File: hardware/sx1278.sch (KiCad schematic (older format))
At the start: 4 parts

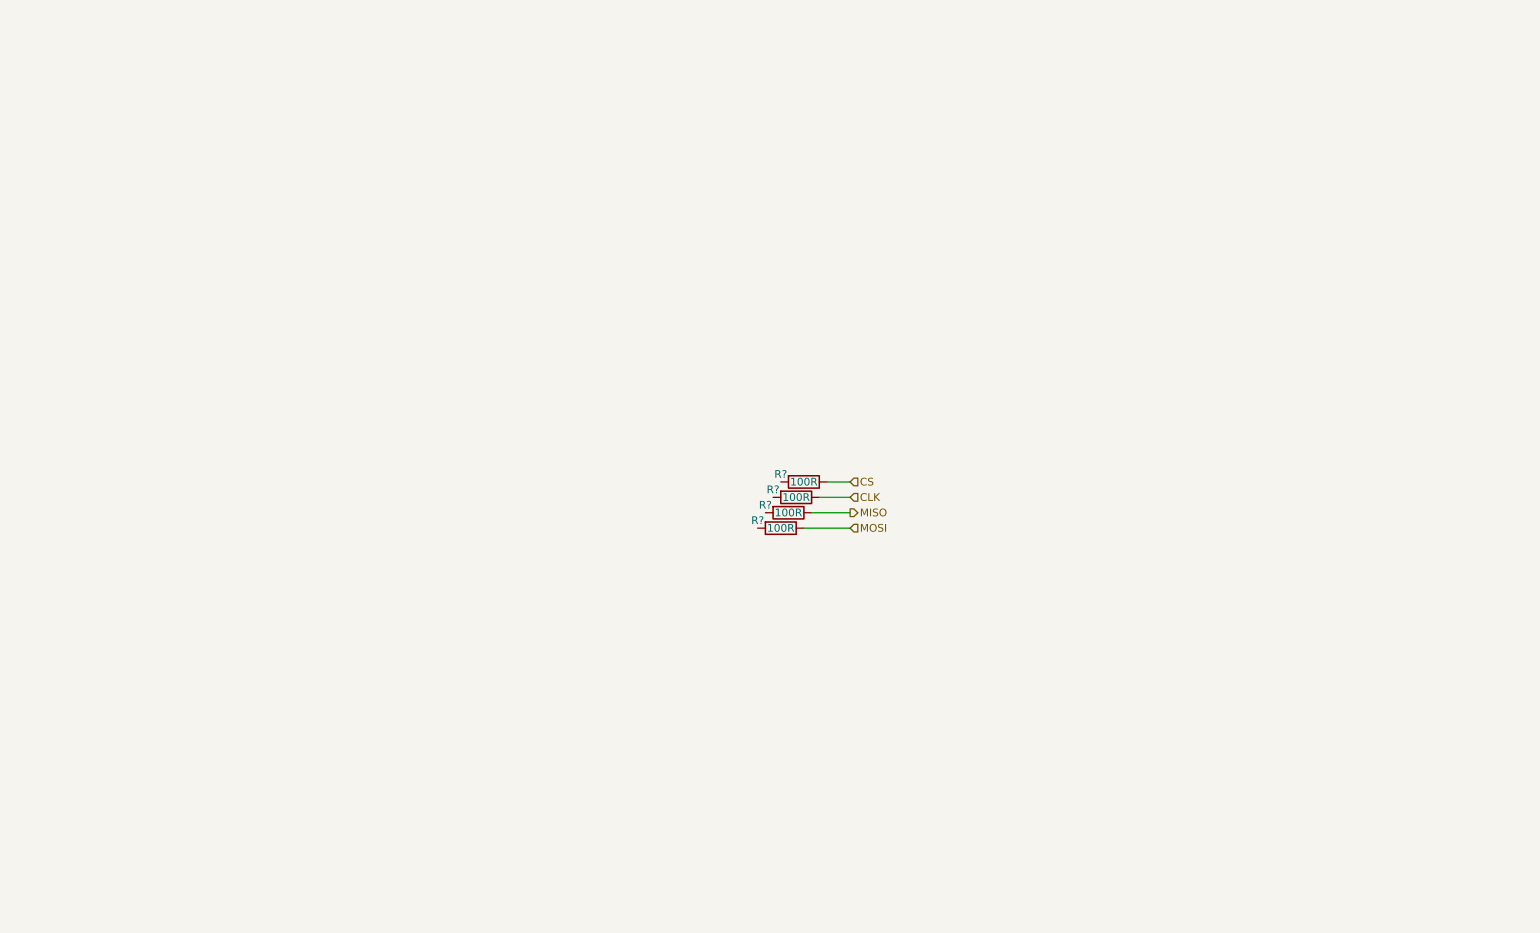
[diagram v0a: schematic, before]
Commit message: Finished sx1278 schematic
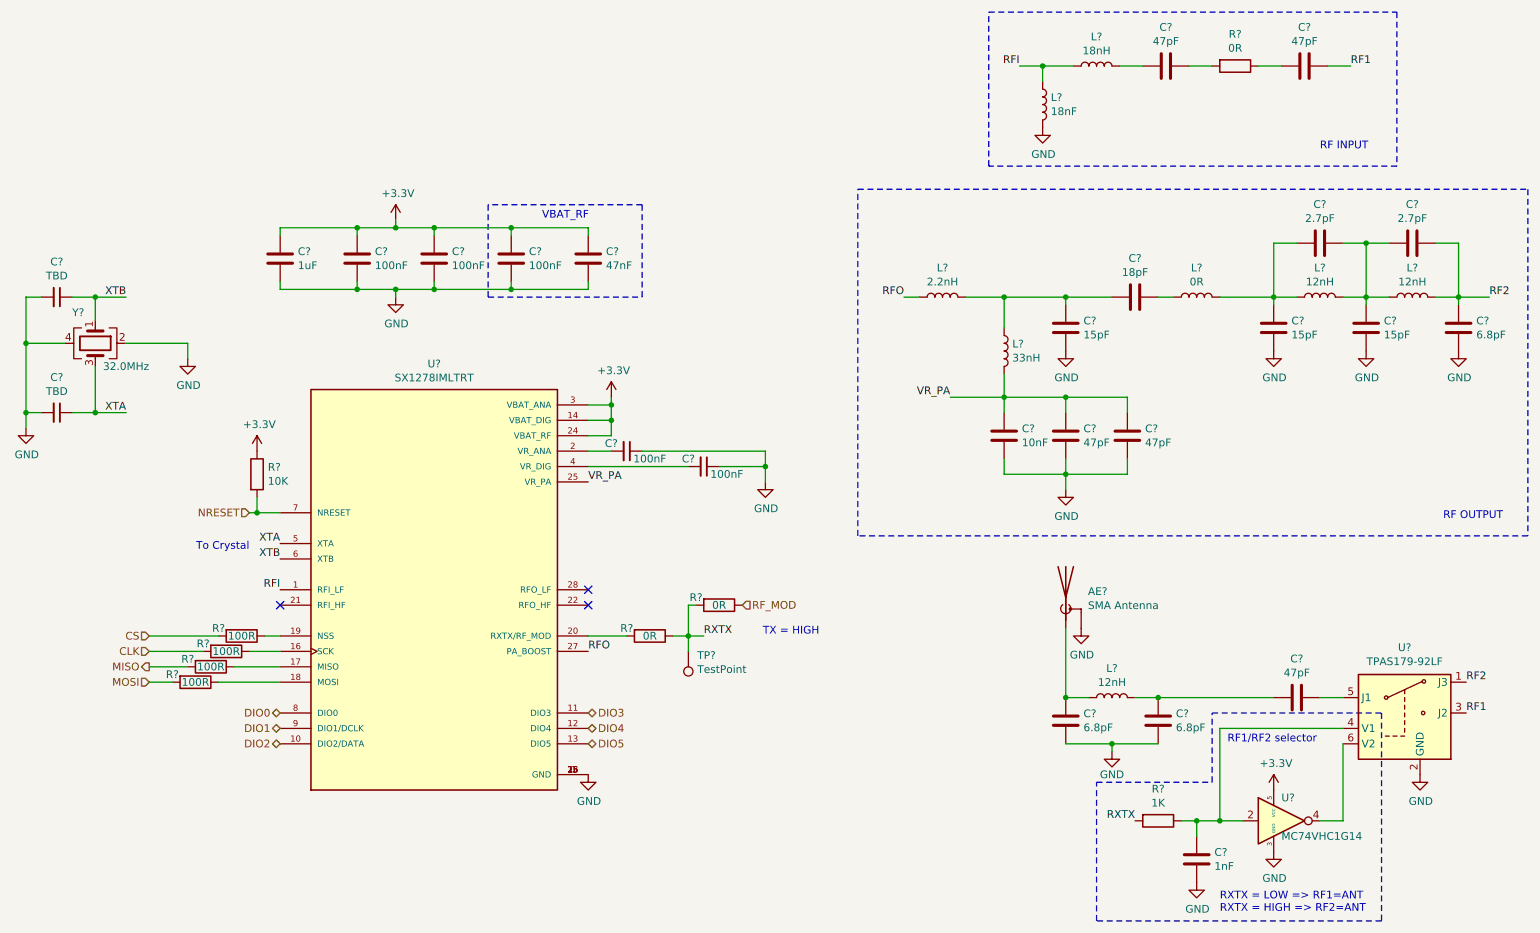
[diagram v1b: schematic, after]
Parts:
- added AE?: SMA Antenna, symbol Device:Antenna_Shield
- added C? (x2): TBD, symbol Device:C_Small
- added C? (x2): 100nF, symbol Device:C_Small
- added C?: 1uF, symbol Device:C
- added C? (x3): 100nF, symbol Device:C
- added C?: 1nF, symbol Device:C
- added C? (x5): 47pF, symbol Device:C
- added C? (x3): 6.8pF, symbol Device:C
- added C?: 10nF, symbol Device:C
- added C?: 47nF, symbol Device:C
- added C? (x3): 15pF, symbol Device:C
- added C?: 18pF, symbol Device:C
- added C? (x2): 2.7pF, symbol Device:C
- added L? (x3): 12nH, symbol Device:L
- added L?: 18nF, symbol Device:L
- added L?: 18nH, symbol Device:L
- added L?: 33nH, symbol Device:L
- added L?: 2.2nH, symbol Device:L
- added L?: 0R, symbol Device:L
- added R?: 10K, symbol Device:R
- added R?: 1K, symbol Device:R
- added R? (x3): 0R, symbol Device:R
- added TP?: TestPoint, symbol Connector:TestPoint
- added U?: SX1278IMLTRT, QFN65P600X600X100-29N, symbol sx1278:SX1278IMLTRT
- added U?: TPAS179-92LF, Package_TO_SOT_SMD:SOT-363_SC-70-6, symbol RF_Switch:AS179-92LF
- added U?: MC74VHC1G14, Package_TO_SOT_SMD:SOT-353_SC-70-5, symbol 74xGxx:NC7SVU04P5X
- added Y?: 32.0MHz, symbol Device:Crystal_GND24
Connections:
- net CLK: now also R?.2; no longer R?.1
- net CS: now also R?.2; no longer R?.1
- net MISO: now also R?.2; no longer R?.1
- net MOSI: now also R?.2; no longer R?.1
- new net: R?.1, U?.16 (SCK)
- new net: R?.1, U?.17 (MISO)
- new net: R?.1, U?.18 (MOSI)
- new net: R?.1, U?.19 (NSS)
- new net: C?.2, U?.2 (VR_ANA)
- new net: R?.2, U?.20 (RXTX/RF_MOD)
- new net: C?.2, U?.4 (VR_DIG)
- new net: AE?.1 (A), C?.1, L?.1
- new net: C?.1, R?.1, U?.2, U?.4 (V1)
- new net: C?.1, U?.5 (J1)
- new net: U?.4, U?.6 (V2)
- new net: C?.1, C?.2, L?.2
- new net: C?.2, L?.2
- new net: C?.1, R?.2
- new net: C?.2, R?.1
- new net: C?.1, C?.2, L?.1, L?.2 (x2)
- new net: C?.1, L?.1
- new net: C?.1, C?.1, C?.2, L?.1, L?.2
- new net +3V3: C?.1, C?.1, C?.1, C?.1, C?.1, R?.1, U?.14 (VBAT_DIG), U?.24 (VBAT_RF), U?.3 (VBAT_ANA), U?.5 (VCC)
- new net DIO0: U?.8 (DIO0)
- new net DIO1: U?.9 (DIO1/DCLK)
- new net DIO2: U?.10 (DIO2/DATA)
- new net DIO3: U?.11 (DIO3)
- new net DIO4: U?.12 (DIO4)
- new net DIO5: U?.13 (DIO5)
- new net GND: AE?.2 (Shield), C?.1, C?.1, C?.2, C?.2, C?.2, C?.2, C?.2, C?.2, C?.2, C?.2, C?.2, C?.2, C?.2, C?.2, C?.2, C?.2, C?.2, C?.2, C?.2, L?.2, U?.0 (GND), U?.15 (GND), U?.2 (GND), U?.23 (GND), U?.26 (GND), U?.3 (GND), Y?.2, Y?.4
- new net NRESET: R?.2, U?.7 (NRESET)
- new net RF1: C?.1, U?.3 (J2)
- new net RF2: C?.1, C?.1, L?.2, U?.1 (J3)
- new net RFI: L?.1, L?.1, U?.1 (RFI_LF)
- new net RFO: L?.1, U?.27 (PA_BOOST)
- new net RF_MOD: R?.1
- new net RXTX: R?.1, R?.2, R?.2, TP?.1
- new net VR_PA: C?.1, C?.1, C?.1, L?.2, U?.25 (VR_PA)
- new net XTA: C?.1, U?.5 (XTA), Y?.3
- new net XTB: C?.1, U?.6 (XTB), Y?.1
- no-connect marks 0 -> 3
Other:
- note added: "RF INPUT"
- note added: "RF OUTPUT"
- note added: "RF1/RF2 selector"
- note added: "RXTX = LOW => RF1=ANT\nRXTX = HIGH => RF2=ANT"
- note added: "TX = HIGH"
- note added: "To Crystal"
- note added: "VBAT_RF"
- moved on the sheet: R?

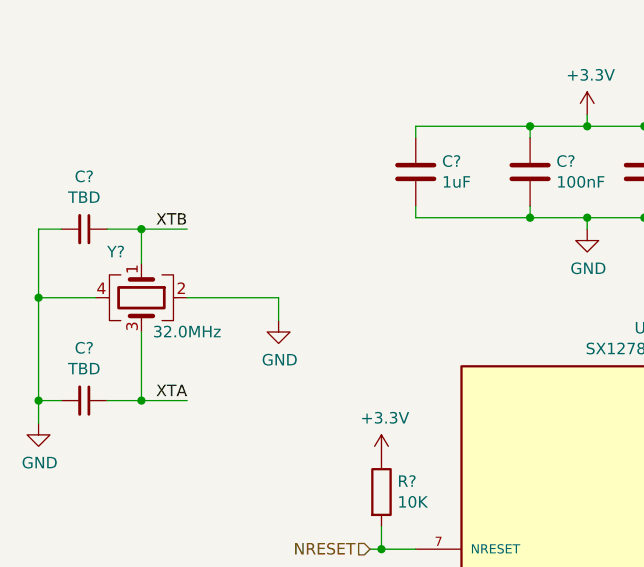
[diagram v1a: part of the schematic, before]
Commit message: Select crystals, add HSE for stm32 and fixed some bits
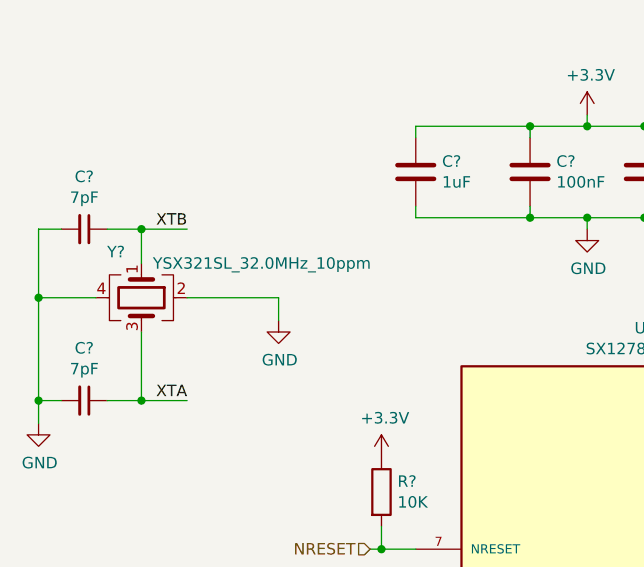
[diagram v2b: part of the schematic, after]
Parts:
- C? (x2): value TBD -> 7pF
- Y?: value 32.0MHz -> YSX321SL_32.0MHz_10ppm; footprint (none) -> Crystal:Crystal_SMD_3225-4Pin_3.2x2.5mm
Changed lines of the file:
@@
 encoding utf-8
 Sheet 4 5
-Title ""
+Title "Meteostation"
 Date ""
 Rev ""
-Comp ""
+Comp "Technospark"
 Comment1 ""
-Comment2 ""
+Comment2 "Aleksul"
 Comment3 ""
 Comment4 ""
@@
 	2150 4900 2550 4900
 $Comp
-L power:GND #PWR?
+L power:GND #PWR0172
 U 1 1 607BCAFD
 P 4550 5500
-F 0 "#PWR?" H 4550 5250 50  0001 C CNN
+F 0 "#PWR0172" H 4550 5250 50  0001 C CNN
 F 1 "GND" H 4555 5327 50  0000 C CNN
 F 2 "" H 4550 5500 50  0001 C CNN
@@
 $EndComp
 $Comp
-L power:+3.3V #PWR?
+L power:+3.3V #PWR0173
 U 1 1 607D9E51
 P 2400 3400
-F 0 "#PWR?" H 2400 3250 50  0001 C CNN
+F 0 "#PWR0173" H 2400 3250 50  0001 C CNN
 F 1 "+3.3V" H 2415 3573 50  0000 C CNN
 F 2 "" H 2400 3400 50  0001 C CNN
@@
 P 1100 3150
 F 0 "C?" V 871 3150 50  0000 C CNN
-F 1 "TBD" V 962 3150 50  0000 C CNN
+F 1 "7pF" V 962 3150 50  0000 C CNN
 F 2 "" H 1100 3150 50  0001 C CNN
 F 3 "~" H 1100 3150 50  0001 C CNN
@@
 P 1100 2400
 F 0 "C?" V 871 2400 50  0000 C CNN
-F 1 "TBD" V 962 2400 50  0000 C CNN
+F 1 "7pF" V 962 2400 50  0000 C CNN
 F 2 "" H 1100 2400 50  0001 C CNN
 F 3 "~" H 1100 2400 50  0001 C CNN
@@
 P 1350 2700
 F 0 "Y?" V 1150 2550 50  0000 L CNN
-F 1 "32.0MHz" V 1500 2750 50  0000 L CNN
-F 2 "" H 1350 2700 50  0001 C CNN
+F 1 "YSX321SL_32.0MHz_10ppm" V 1200 2750 50  0000 L CNN
+F 2 "Crystal:Crystal_SMD_3225-4Pin_3.2x2.5mm" H 1350 2700 50  0001 C CNN
 F 3 "~" H 1350 2700 50  0001 C CNN
 	1    1350 2700
@@
 Connection ~ 1350 2400
 $Comp
-L power:GND #PWR?
+L power:GND #PWR0174
 U 1 1 607F6B66
 P 1950 2800
-F 0 "#PWR?" H 1950 2550 50  0001 C CNN
+F 0 "#PWR0174" H 1950 2550 50  0001 C CNN
 F 1 "GND" H 1955 2627 50  0000 C CNN
 F 2 "" H 1950 2800 50  0001 C CNN
@@
 	1950 2700 1550 2700
 $Comp
-L power:GND #PWR?
+L power:GND #PWR0175
 U 1 1 607FA960
 P 900 3250
-F 0 "#PWR?" H 900 3000 50  0001 C CNN
+F 0 "#PWR0175" H 900 3000 50  0001 C CNN
 F 1 "GND" H 905 3077 50  0000 C CNN
 F 2 "" H 900 3250 50  0001 C CNN
@@
 $EndComp
 $Comp
-L power:GND #PWR?
+L power:GND #PWR0176
 U 1 1 608065FD
 P 5700 3600
-F 0 "#PWR?" H 5700 3350 50  0001 C CNN
+F 0 "#PWR0176" H 5700 3350 50  0001 C CNN
 F 1 "GND" H 5705 3427 50  0000 C CNN
 F 2 "" H 5700 3600 50  0001 C CNN
@@
 $EndComp
 $Comp
-L power:+3.3V #PWR?
+L power:+3.3V #PWR0177
 U 1 1 6080AC31
 P 3300 1900
-F 0 "#PWR?" H 3300 1750 50  0001 C CNN
+F 0 "#PWR0177" H 3300 1750 50  0001 C CNN
 F 1 "+3.3V" H 3315 2073 50  0000 C CNN
 F 2 "" H 3300 1900 50  0001 C CNN
@@
 $EndComp
 $Comp
-L power:GND #PWR?
+L power:GND #PWR0178
 U 1 1 6080CCB3
 P 3300 2400
-F 0 "#PWR?" H 3300 2150 50  0001 C CNN
+F 0 "#PWR0178" H 3300 2150 50  0001 C CNN
 F 1 "GND" H 3305 2227 50  0000 C CNN
 F 2 "" H 3300 2400 50  0001 C CNN
@@
 Connection ~ 3050 1950
 $Comp
-L power:+3.3V #PWR?
+L power:+3.3V #PWR0179
 U 1 1 608179F3
 P 4700 3050
-F 0 "#PWR?" H 4700 2900 50  0001 C CNN
+F 0 "#PWR0179" H 4700 2900 50  0001 C CNN
 F 1 "+3.3V" H 4715 3223 50  0000 C CNN
 F 2 "" H 4700 3050 50  0001 C CNN
@@
 $EndComp
 $Comp
-L power:GND #PWR?
+L power:GND #PWR0180
 U 1 1 6083FC11
 P 7750 4550
-F 0 "#PWR?" H 7750 4300 50  0001 C CNN
+F 0 "#PWR0180" H 7750 4300 50  0001 C CNN
 F 1 "GND" H 7755 4377 50  0000 C CNN
 F 2 "" H 7750 4550 50  0001 C CNN
@@
 $EndComp
 $Comp
-L power:GND #PWR?
+L power:GND #PWR0181
 U 1 1 60845D96
 P 9950 5500
-F 0 "#PWR?" H 9950 5250 50  0001 C CNN
+F 0 "#PWR0181" H 9950 5250 50  0001 C CNN
 F 1 "GND" H 9955 5327 50  0000 C CNN
 F 2 "" H 9950 5500 50  0001 C CNN
@@
 $EndComp
 $Comp
-L power:GND #PWR?
+L power:GND #PWR0182
 U 1 1 6084BC05
 P 9000 6000
-F 0 "#PWR?" H 9000 5750 50  0001 C CNN
+F 0 "#PWR0182" H 9000 5750 50  0001 C CNN
 F 1 "GND" H 9005 5827 50  0000 C CNN
 F 2 "" H 9000 6000 50  0001 C CNN
@@
 $EndComp
 $Comp
-L power:+3.3V #PWR?
+L power:+3.3V #PWR0183
 U 1 1 6084BF68
 P 9000 5600
-F 0 "#PWR?" H 9000 5450 50  0001 C CNN
+F 0 "#PWR0183" H 9000 5450 50  0001 C CNN
 F 1 "+3.3V" H 9015 5773 50  0000 C CNN
 F 2 "" H 9000 5600 50  0001 C CNN
@@
 $EndComp
 $Comp
-L power:GND #PWR?
+L power:GND #PWR0184
 U 1 1 60862585
 P 8500 6200
-F 0 "#PWR?" H 8500 5950 50  0001 C CNN
+F 0 "#PWR0184" H 8500 5950 50  0001 C CNN
 F 1 "GND" H 8505 6027 50  0000 C CNN
 F 2 "" H 8500 6200 50  0001 C CNN
@@
 	8250 5000 9000 5000
 $Comp
-L power:GND #PWR?
+L power:GND #PWR0185
 U 1 1 608A4F1C
 P 7950 5350
-F 0 "#PWR?" H 7950 5100 50  0001 C CNN
+F 0 "#PWR0185" H 7950 5100 50  0001 C CNN
 F 1 "GND" H 7950 5200 50  0000 C CNN
 F 2 "" H 7950 5350 50  0001 C CNN
@@
 RF1
 $Comp
-L power:GND #PWR?
+L power:GND #PWR0186
 U 1 1 608B75C0
 P 7500 1300
-F 0 "#PWR?" H 7500 1050 50  0001 C CNN
+F 0 "#PWR0186" H 7500 1050 50  0001 C CNN
 F 1 "GND" H 7505 1127 50  0000 C CNN
 F 2 "" H 7500 1300 50  0001 C CNN
@@
 Connection ~ 7650 3050
 $Comp
-L power:GND #PWR?
+L power:GND #PWR0187
 U 1 1 608E8BAF
 P 7650 3650
-F 0 "#PWR?" H 7650 3400 50  0001 C CNN
+F 0 "#PWR0187" H 7650 3400 50  0001 C CNN
 F 1 "GND" H 7655 3477 50  0000 C CNN
 F 2 "" H 7650 3650 50  0001 C CNN
@@
 $EndComp
 $Comp
-L power:GND #PWR?
+L power:GND #PWR0188
 U 1 1 60909ED7
 P 7650 2750
-F 0 "#PWR?" H 7650 2500 50  0001 C CNN
+F 0 "#PWR0188" H 7650 2500 50  0001 C CNN
 F 1 "GND" H 7655 2577 50  0000 C CNN
 F 2 "" H 7650 2750 50  0001 C CNN
@@
 Connection ~ 10200 2400
 $Comp
-L power:GND #PWR?
+L power:GND #PWR0189
 U 1 1 609445A2
 P 9000 2750
-F 0 "#PWR?" H 9000 2500 50  0001 C CNN
+F 0 "#PWR0189" H 9000 2500 50  0001 C CNN
 F 1 "GND" H 9005 2577 50  0000 C CNN
 F 2 "" H 9000 2750 50  0001 C CNN
@@
 $EndComp
 $Comp
-L power:GND #PWR?
+L power:GND #PWR0190
 U 1 1 60945D29
 P 9600 2750
-F 0 "#PWR?" H 9600 2500 50  0001 C CNN
+F 0 "#PWR0190" H 9600 2500 50  0001 C CNN
 F 1 "GND" H 9605 2577 50  0000 C CNN
 F 2 "" H 9600 2750 50  0001 C CNN
@@
 $EndComp
 $Comp
-L power:GND #PWR?
+L power:GND #PWR0191
 U 1 1 6094646B
 P 10200 2750
-F 0 "#PWR?" H 10200 2500 50  0001 C CNN
+F 0 "#PWR0191" H 10200 2500 50  0001 C CNN
 F 1 "GND" H 10205 2577 50  0000 C CNN
 F 2 "" H 10200 2750 50  0001 C CNN

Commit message: Annotation complete
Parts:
- gave numbers to parts that had none: 48

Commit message: Finish adding footprints
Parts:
- AE2: footprint (none) -> Connector_Coaxial:SMA_Molex_73251-2200_Horizontal
- C35, C36, C37, C38, C40, C41, C42, C43, C44, C45, C46, C47, C48, C49, C50, C51, C52, C53, C54, C55, C56, C57, C58, C59: footprint (none) -> Capacitor_SMD:C_0805_2012Metric
- C39: footprint (none) -> Capacitor_SMD:C_1206_3216Metric
- L10, L11, L4, L6, L8, L9: footprint (none) -> Inductor_SMD:L_0603_1608Metric
- L5: value 18nF -> 18nH; footprint (none) -> Inductor_SMD:L_0603_1608Metric
- L7, R45, R47, R49: footprint (none) -> Resistor_SMD:R_2512_6332Metric
- R46, R48, R50, R51, R52, R53: footprint (none) -> Resistor_SMD:R_0805_2012Metric
- TP1: footprint (none) -> TestPoint:TestPoint_Pad_D2.5mm
- U8: footprint QFN65P600X600X100-29N -> libs:QFN65P600X600X100-29N

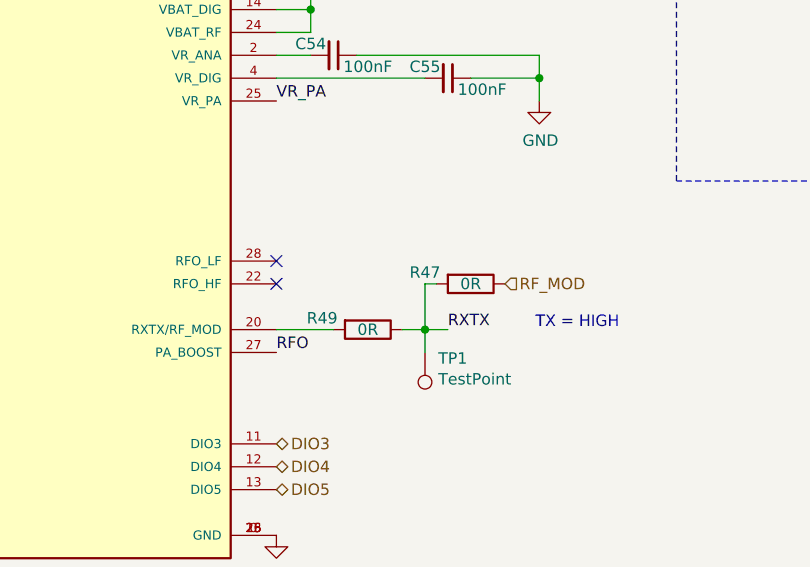
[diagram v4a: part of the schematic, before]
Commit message: Change 0Rto solder jumpers Add 3d model for bq25895 Fix button pcb model Start power part of pcb
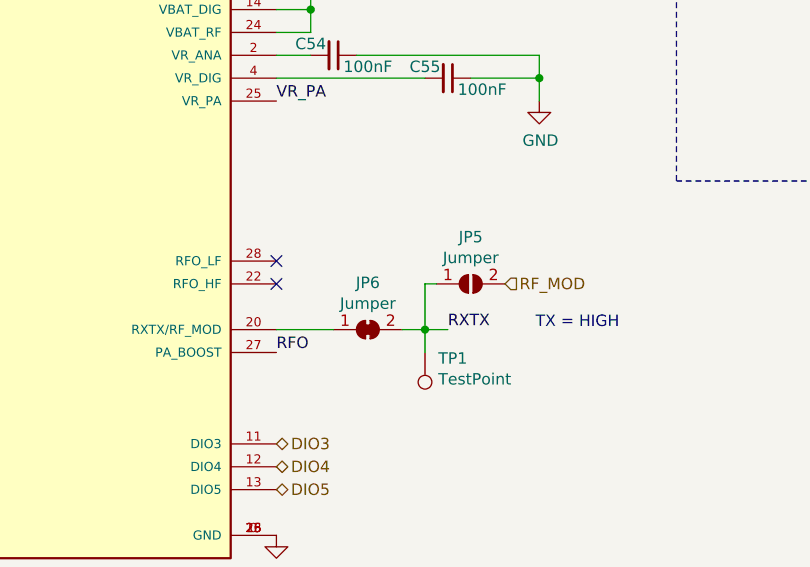
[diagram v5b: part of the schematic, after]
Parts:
- removed R47, R49: 0R, Resistor_SMD:R_2512_6332Metric, symbol Device:R
- added JP5: Jumper, Jumper:SolderJumper-2_P1.3mm_Open_RoundedPad1.0x1.5mm, symbol Jumper:SolderJumper_2_Open
- added JP6: Jumper, Jumper:SolderJumper-2_P1.3mm_Bridged2Bar_Pad1.0x1.5mm, symbol Jumper:SolderJumper_2_Bridged
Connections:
- net RF_MOD: now also JP5.2 (B)
- net RXTX: now also JP5.1 (A), JP6.2 (B)
- net at U8.20 (RXTX/RF_MOD): now also JP6.1 (A)
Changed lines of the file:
@@
 Connection ~ 8650 5800
 Connection ~ 8500 5800
-$Comp
-L Device:R R49
-U 1 1 608731D9
-P 4950 4600
-F 0 "R49" V 4900 4400 50  0000 C CNN
-F 1 "0R" V 4950 4600 50  0000 C CNN
-F 2 "Resistor_SMD:R_2512_6332Metric" V 4880 4600 50  0001 C CNN
-F 3 "~" H 4950 4600 50  0001 C CNN
-	1    4950 4600
-	0    1    1    0
-$EndComp
-$Comp
-L Device:R R47
-U 1 1 6087422D
-P 5400 4400
-F 0 "R47" V 5350 4200 50  0000 C CNN
-F 1 "0R" V 5400 4400 50  0000 C CNN
-F 2 "Resistor_SMD:R_2512_6332Metric" V 5330 4400 50  0001 C CNN
-F 3 "~" H 5400 4400 50  0001 C CNN
-	1    5400 4400
-	0    1    1    0
-$EndComp
 Text HLabel 5550 4400 2    50   Input ~ 0
 RF_MOD
@@
 Text HLabel 4550 5300 2    50   BiDi ~ 0
 DIO5
+$Comp
+L Jumper:SolderJumper_2_Open JP5
+U 1 1 608ED2EB
+P 5400 4400
+F 0 "JP5" H 5400 4605 50  0000 C CNN
+F 1 "Jumper" H 5400 4514 50  0000 C CNN
+F 2 "Jumper:SolderJumper-2_P1.3mm_Open_RoundedPad1.0x1.5mm" H 5400 4400 50  0001 C CNN
+F 3 "~" H 5400 4400 50  0001 C CNN
+	1    5400 4400
+	1    0    0    -1
+$EndComp
+$Comp
+L Jumper:SolderJumper_2_Bridged JP6
+U 1 1 608EF9C2
+P 4950 4600
+F 0 "JP6" H 4950 4805 50  0000 C CNN
+F 1 "Jumper" H 4950 4714 50  0000 C CNN
+F 2 "Jumper:SolderJumper-2_P1.3mm_Bridged2Bar_Pad1.0x1.5mm" H 4950 4600 50  0001 C CNN
+F 3 "~" H 4950 4600 50  0001 C CNN
+	1    4950 4600
+	1    0    0    -1
+$EndComp
 $EndSCHEMATC
